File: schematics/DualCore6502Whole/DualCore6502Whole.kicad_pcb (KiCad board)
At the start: 2 copper layers, 72 parts, among them J1 VIN, J2 PWR, J3 PORTA/PORTB, J4 RS232, J5 Bus 1, SW1 Power, SW2 RESET, U1 LM7805, U10 62256, U11 28C256, U12 74HC00, U13 74HC138, U14 74HC374, U15 W65C22N, U16 W65C51N, U17 MAX232, U18 74HC00, U2 W65C02S, U3 74HC157, U4 W65C02S, U5 74HC08, U6 74HC02, U7 74HC32, U8 74HC4017, U9 74HC86, Y1 12MHz, Y2 1.8432MHz

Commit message: Remove the need to multiplex the control lines
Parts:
- removed the C5 at (284.8, 117.5)
- removed the U3 at (149.9, 121.9)
- renumbered C11 to C10, C12 to C11, C13 to C12, C14 to C13, C15 to C14, C16 to C15, C17 to C16, C18 to C17, C19 to C18, C20 to C19, C21 to C20, C22 to C21, C23 to C22, C24 to C23, C6 to C5, C7 to C6, C8 to C7, C9 to C8, C10 to C9, U11 to U10, U12 to U11, U13 to U12, U14 to U13, U15 to U14, U16 to U15, U17 to U16, U18 to U17, U4 to U3, U5 to U4, U6 to U5, U7 to U6, U8 to U7, U9 to U8, U10 to U9
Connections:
- J5 pad 47: SYNC -> unconnected-(J5-Pin_47-Pad47)
- J5 pad 48: ~{VP} -> unconnected-(J5-Pin_48-Pad48)
- U10 pad 1: CPU_ID -> CPU2_BUSEN
- U2 pad 34: CPU1_R/~{W} -> R/~{W}
- U3 pad 34: CPU2_R/~{W} -> R/~{W}
- U6 pad 12: CPU1_CLK -> CPU2_CLK
- U6 pad 13: CPU2_CLK -> CPU1_CLK
- U8 pad 13: CPU_ID -> CPU2_BUSEN

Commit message: Update the schematic
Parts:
- removed the C8 at (277.3, 165.3)
- removed the U4 at (101.6, 45.7)
- added C16: 100nF, Capacitor_THT:C_Disc_D5.0mm_W2.5mm_P5.00mm, F.Cu at (369.1, 177.9)
- added C17: 100nF, Capacitor_THT:C_Disc_D5.0mm_W2.5mm_P5.00mm, F.Cu at (369.1, 181.9)
- added C18: 100nF, Capacitor_THT:C_Disc_D5.0mm_W2.5mm_P5.00mm, F.Cu at (369.1, 186.0)
- added C19: 100nF, Capacitor_THT:C_Disc_D5.0mm_W2.5mm_P5.00mm, F.Cu at (369.1, 190.1)
- added C20: 100nF, Capacitor_THT:C_Disc_D5.0mm_W2.5mm_P5.00mm, F.Cu at (369.1, 194.1)
- added C9: 100nF, Capacitor_THT:C_Disc_D5.0mm_W2.5mm_P5.00mm, F.Cu at (363.2, 203.2)
- added D3: IND4, LED_THT:LED_D3.0mm, F.Cu at (352.4, 174.6)
- added D4: IND3, LED_THT:LED_D3.0mm, F.Cu at (352.4, 180.0)
- added D5: IND2, LED_THT:LED_D3.0mm, F.Cu at (352.4, 185.5)
- added D6: IND1, LED_THT:LED_D3.0mm, F.Cu at (352.4, 191.0)
- added D7: IND0, LED_THT:LED_D3.0mm, F.Cu at (352.4, 196.4)
- added J3: Aux Inputs, Connector_PinHeader_2.54mm:PinHeader_2x05_P2.54mm_Vertical, F.Cu at (396.5, 154.8)
- added JP1: VIA IRQ, Connector_PinHeader_2.54mm:PinHeader_1x03_P2.54mm_Vertical, F.Cu at (374.1, 209.6)
- added JP2: ACIA IRQ, Connector_PinHeader_2.54mm:PinHeader_1x03_P2.54mm_Vertical, F.Cu at (380.7, 209.6)
- added R10: 470R, Resistor_THT:R_Axial_DIN0207_L6.3mm_D2.5mm_P10.16mm_Horizontal, F.Cu at (388.1, 177.9)
- added R11: 470R, Resistor_THT:R_Axial_DIN0207_L6.3mm_D2.5mm_P10.16mm_Horizontal, F.Cu at (388.1, 181.9)
- added R12: 470R, Resistor_THT:R_Axial_DIN0207_L6.3mm_D2.5mm_P10.16mm_Horizontal, F.Cu at (388.1, 186.0)
- added R13: 470R, Resistor_THT:R_Axial_DIN0207_L6.3mm_D2.5mm_P10.16mm_Horizontal, F.Cu at (388.1, 190.1)
- added R5: 1K, Resistor_THT:R_Axial_DIN0207_L6.3mm_D2.5mm_P10.16mm_Horizontal, F.Cu at (373.3, 203.2)
- added R8: 1K, Resistor_THT:R_Axial_DIN0207_L6.3mm_D2.5mm_P10.16mm_Horizontal, F.Cu at (388.6, 203.2)
- added R9: 470R, Resistor_THT:R_Axial_DIN0207_L6.3mm_D2.5mm_P10.16mm_Horizontal, F.Cu at (388.1, 173.8)
- added U14: 74HC259, Package_DIP:DIP-16_W7.62mm, F.Cu at (377.2, 173.9)
- added U15: 74HC245, Package_DIP:DIP-20_W7.62mm, F.Cu at (358.2, 173.9)
- added U16: 74HC00, Package_DIP:DIP-14_W7.62mm, F.Cu at (363.2, 154.5)
- added U17: 74HC08, Package_DIP:DIP-14_W7.62mm, F.Cu at (374.1, 154.5)
- added U18: 74HC74, Package_DIP:DIP-14_W7.62mm, F.Cu at (384.9, 154.5)
- added U7: 74HC138, Package_DIP:DIP-16_W7.62mm, F.Cu at (352.4, 203.2)
- U13: value 74HC374 -> 74HC10; footprint Package_DIP:DIP-20_W7.62mm -> Package_DIP:DIP-14_W7.62mm
- moved U13 315.9 mm to (352.4, 154.5), turned to 0 degrees
- moved J6 287.7 mm to (190.5, 43.2)
- moved C15 152.9 mm to (369.1, 173.8)
- moved U9 86.5 mm to (132.1, 96.5)
- moved U2 61.2 mm to (58.4, 71.1)
- moved SW2 54.1 mm to (57.4, 46.2)
- moved C3 54.1 mm to (53.3, 38.0)
- moved R2 54.1 mm to (53.3, 51.3)
- moved J4 45.0 mm to (45.7, 208.3)
- moved U19 45.0 mm to (53.3, 198.1)
- moved U20 45.0 mm to (119.4, 198.1)
- moved U21 45.0 mm to (162.6, 193.0)
- moved U10 30.6 mm to (68.6, 96.5)
- moved U3 30.6 mm to (116.8, 71.1)
- moved Y1 27.9 mm to (76.2, 45.7)
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- renumbered C16 to C21, C17 to C22, C18 to C23, C19 to C24, C20 to C25, C21 to C26, C22 to C27, C23 to C28, C9 to C8, D3 to D8, D4 to D9, J3 to J4, J4 to J5, J5 to J6, R9 to R14, R10 to R15, R11 to R16, R12 to R17, R13 to R18, R14 to R19, U14 to U19, U15 to U20, U16 to U21, U17 to U22, U5 to U4, U6 to U5, U7 to U6
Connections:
- net Net-(U7-CLK) renamed MAIN_CLK
- D8 pad 2: ~{CPU1_IRQ} -> Net-(D8-A)
- D9 pad 2: ~{CPU2_IRQ} -> Net-(D9-A)
- J5 pad 7: unconnected-(J4-Pad7) -> Net-(U21-R2IN)
- U11 pad 4: A14 -> A15
- U11 pad 5: +5V -> Net-(U11-Pad5)
- U13 pad 1: Net-(U13-OE) -> COMMON_CLK
- U13 pad 10: GND -> Net-(U13-Pad10)
- U13 pad 11: Net-(U13-Cp) -> A8
- U13 pad 12: D4 -> Net-(U15-CE)
- U13 pad 13: D4 -> A7
- U13 pad 14: D5 -> +5V
- U13 pad 2: D0 -> Net-(U13-Pad10)
- U13 pad 3: D0 -> ~{MUTEX_CS}
- U13 pad 4: D1 -> +5V
- U13 pad 5: D1 -> +5V
- U13 pad 6: D2 -> Net-(U13-Pad10)
- U13 pad 7: D2 -> GND
- U13 pad 8: D3 -> Net-(U14-E)
- U13 pad 9: D3 -> COMMON_CLK
- U19 pad 25: CPU1_CLK -> COMMON_CLK
- U20 pad 27: CPU2_CLK -> COMMON_CLK
- U20 pad 8: Net-(U15-~{RTS}) -> unconnected-(U20-~{RTS}-Pad8)
- U21 pad 10: Net-(U15-~{RTS}) -> ~{RTS}
- U21 pad 8: unconnected-(U16-R2IN-Pad8) -> Net-(U21-R2IN)
- U21 pad 9: unconnected-(U16-R2OUT-Pad9) -> ~{CTS}
- U22 pad 13: R/~{W} -> +5V
- U4 pad 10: Net-(U13-Cp) -> unconnected-(U4-Pad10)
- U4 pad 11: R/~{W} -> +5V
- U4 pad 12: GND -> +5V
- U4 pad 13: Net-(U5-Pad13) -> unconnected-(U4-Pad13)
- U4 pad 2: Net-(U4-Pad11) -> BUSEN_RESET
- U4 pad 6: Net-(U4-Pad8) -> BUSEN_SET
- U4 pad 8: ~{MUTEX_CS} -> +5V
- U4 pad 9: R/~{W} -> +5V
- U5 pad 1: ~{CPU1_ML} -> CPU1_CLK_RAW
- U5 pad 10: Net-(U5-Pad13) -> CPU2_CLK_RAW
- U5 pad 12: CPU2_CLK -> CPU2_CLK_RAW
- U5 pad 13: CPU1_CLK -> CPU1_CLK_RAW
- U5 pad 2: ~{MUTEX_CS} -> GND
- U5 pad 3: CPU2_RDY -> CPU1_CLK
- U5 pad 4: ~{CPU2_ML} -> GND
- U5 pad 5: ~{MUTEX_CS} -> GND
- U5 pad 6: CPU1_RDY -> unconnected-(U5-Pad6)
- U5 pad 8: Net-(U13-OE) -> CPU2_CLK
- U5 pad 9: ~{MUTEX_CS} -> GND
- U6 pad 10: CPU2_CLK -> CPU2_CLK_RAW
- U6 pad 2: CPU1_CLK -> CPU1_CLK_RAW
- U8 pad 1: GND -> A14
- U8 pad 10: GND -> +5V
- U8 pad 11: Net-(U9-A14) -> Net-(U9-A9)
- U8 pad 12: A14 -> A9
- U8 pad 13: CPU2_BUSEN -> Net-(U8-Pad13)
- U8 pad 2: GND -> +5V
- U8 pad 3: unconnected-(U8-Pad3) -> Net-(U11-Pad5)
- U8 pad 4: GND -> +5V
- U8 pad 5: GND -> Net-(U11-Pad6)
- U8 pad 6: unconnected-(U8-Pad6) -> IO_CS
- U8 pad 8: unconnected-(U8-Pad8) -> Net-(U8-Pad13)
- U8 pad 9: GND -> Net-(U7-O0)
- U9 pad 1: Net-(U9-A14) -> A14
- U9 pad 24: A9 -> Net-(U9-A9)
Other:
- board outline added: 160 x 121.9 mm

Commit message: Basic PCB layout
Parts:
- removed the C2 at (390.9, 43.1)
- removed the D1 at (377.9, 38.9)
- removed the U1 at (367.7, 44.4)
- added C28: 10nF, Capacitor_THT:C_Disc_D5.0mm_W2.5mm_P5.00mm, F.Cu at (143.5, 39.5)
- added C29: 100nF, Capacitor_THT:C_Disc_D5.0mm_W2.5mm_P5.00mm, F.Cu at (158.8, 38.1)
- added JP3: NMI2, Connector_PinHeader_2.54mm:PinHeader_1x02_P2.54mm_Vertical, F.Cu at (142.2, 73.7)
- added R20: 5K6, Resistor_THT:R_Axial_DIN0207_L6.3mm_D2.5mm_P10.16mm_Horizontal, F.Cu at (171.4, 47.0)
- added R21: 2K2, Resistor_THT:R_Axial_DIN0207_L6.3mm_D2.5mm_P10.16mm_Horizontal, F.Cu at (167.6, 36.8)
- added RV1: 10K, Potentiometer_THT:Potentiometer_Bourns_3266Y_Vertical, F.Cu at (163.8, 44.4)
- added TP1: CPU1 SYNC, TestPoint:TestPoint_Pad_D1.5mm, F.Cu at (57.1, 69.9)
- added TP2: ~{CPU1_VP}, TestPoint:TestPoint_Pad_D1.5mm, F.Cu at (64.8, 69.9)
- added TP3: ~{CPU1_ML}, TestPoint:TestPoint_Pad_D1.5mm, F.Cu at (61.0, 69.9)
- added TP4: CPU2 SYNC, TestPoint:TestPoint_Pad_D1.5mm, F.Cu at (120.7, 69.9)
- added TP5: ~{CPU2_VP}, TestPoint:TestPoint_Pad_D1.5mm, F.Cu at (128.3, 69.9)
- added TP6: ~{CPU2_ML}, TestPoint:TestPoint_Pad_D1.5mm, F.Cu at (124.5, 69.9)
- added TP7: 1KHz, TestPoint:TestPoint_Pad_D1.5mm, F.Cu at (152.4, 49.5)
- added U22: 7555, Package_DIP:DIP-8_W7.62mm_Socket, F.Cu at (147.3, 45.7)
- C1: value 47uF -> 100uF
- D1: renamed from D2; value Power On -> Power
- J1: value VIN -> 5VDC
- J2: footprint Connector_PinHeader_2.54mm:PinHeader_1x04_P2.54mm_Vertical -> Connector_Phoenix_MC_HighVoltage:PhoenixContact_MC_1,5_3-G-5.08_1x03_P5.08mm_Horizontal
- J6: value Bus 1 -> RCBus; footprint RCBus:RCBus_PinSocket_2x40_P2.54mm_Vertical -> RCBus:RCBus_PinSocket_2x40_P2.54mm_Vertical_DC
- JP2: value ACIA IRQ -> NMI1; footprint Connector_PinHeader_2.54mm:PinHeader_1x03_P2.54mm_Vertical -> Connector_PinHeader_2.54mm:PinHeader_1x02_P2.54mm_Vertical
- R1: value 220R -> 470R
- SW1: value Power -> Power On
- U1: renamed from U2; footprint Package_DIP:DIP-40_W15.24mm -> Package_DIP:DIP-40_W15.24mm_Socket
- U10: renamed from U11; footprint Package_DIP:DIP-14_W7.62mm -> Package_DIP:DIP-14_W7.62mm_Socket
- U11: renamed from U12; footprint Package_DIP:DIP-16_W7.62mm -> Package_DIP:DIP-16_W7.62mm_Socket
- U12: renamed from U13; footprint Package_DIP:DIP-14_W7.62mm -> Package_DIP:DIP-14_W7.62mm_Socket
- U13: renamed from U14; footprint Package_DIP:DIP-16_W7.62mm -> Package_DIP:DIP-16_W7.62mm_Socket
- U14: renamed from U15; footprint Package_DIP:DIP-20_W7.62mm -> Package_DIP:DIP-20_W7.62mm_Socket
- U15: renamed from U16; footprint Package_DIP:DIP-14_W7.62mm -> Package_DIP:DIP-14_W7.62mm_Socket
- U16: renamed from U17; footprint Package_DIP:DIP-14_W7.62mm -> Package_DIP:DIP-14_W7.62mm_Socket
- U17: renamed from U18; footprint Package_DIP:DIP-14_W7.62mm -> Package_DIP:DIP-14_W7.62mm_Socket
- U18: renamed from U19; footprint Package_DIP:DIP-40_W15.24mm -> Package_DIP:DIP-40_W15.24mm_Socket
- U19: renamed from U20; footprint Package_DIP:DIP-28_W15.24mm -> Package_DIP:DIP-28_W15.24mm_Socket
- U2: renamed from U3; footprint Package_DIP:DIP-40_W15.24mm -> Package_DIP:DIP-40_W15.24mm_Socket
- U20: renamed from U21; footprint Package_DIP:DIP-16_W7.62mm -> Package_DIP:DIP-16_W7.62mm_Socket
- U21: renamed from U22; footprint Package_DIP:DIP-14_W7.62mm -> Package_DIP:DIP-14_W7.62mm_Socket
- U3: renamed from U5; footprint Package_DIP:DIP-14_W7.62mm -> Package_DIP:DIP-14_W7.62mm_Socket
- U4: footprint Package_DIP:DIP-14_W7.62mm -> Package_DIP:DIP-14_W7.62mm_Socket
- U5: renamed from U6; footprint Package_DIP:DIP-16_W7.62mm -> Package_DIP:DIP-16_W7.62mm_Socket
- U6: renamed from U7; footprint Package_DIP:DIP-16_W7.62mm -> Package_DIP:DIP-16_W7.62mm_Socket
- U7: renamed from U8; footprint Package_DIP:DIP-14_W7.62mm -> Package_DIP:DIP-14_W7.62mm_Socket
- U8: renamed from U9; footprint Package_DIP:DIP-28_W15.24mm -> Package_DIP:DIP-28_W15.24mm_Socket
- Y2: footprint Crystal:Crystal_HC49-U_Horizontal -> Crystal:Crystal_HC49-U_Vertical
- moved Y2 405.1 mm to (67.3, 128.3), turned to 180 degrees
- moved D8 398.9 mm to (53.3, 55.9), turned to -90 degrees
- moved C22 397.2 mm to (52.1, 128.3)
- moved SW1 367.6 mm to (34.3, 129.5)
- moved J1 365.3 mm to (44.5, 146.4)
- moved J5 363.0 mm to (127.7, 152.7)
- moved C21 359.6 mm to (87.6, 111.7), turned to 90 degrees
- moved C23 355.7 mm to (91.5, 119.4)
- moved C26 353.4 mm to (91.5, 123.2)
- moved R5 348.8 mm to (57.1, 55.9), turned to -90 degrees
- moved C24 348.4 mm to (99.1, 123.2)
- moved R14 346.3 mm to (82.5, 128.3), turned to 180 degrees
- moved C25 346.1 mm to (99.1, 119.4)
- moved J2 343.8 mm to (39.4, 109.2), turned to -90 degrees
- moved H4 343.4 mm to (34.3, 157.5)
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- renumbered C11 to C10, C12 to C11, C13 to C12, C14 to C13, C15 to C14, C16 to C15, C17 to C16, C18 to C17, C19 to C18, C20 to C19, C3 to C2, C21 to C20, C22 to C21, C23 to C22, C24 to C23, C25 to C24, C26 to C25, C27 to C26, C28 to C27, C4 to C3, C5 to C4, C6 to C5, C7 to C6, C8 to C7, C9 to C8, C10 to C9, D3 to D2, D4 to D3, D5 to D4, D6 to D5, D7 to D6, D8 to D7, D9 to D8, U10 to U9
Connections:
- C1 pad 1: Net-(D1-K) -> +5V
- D8 pad 2: Net-(D9-A) -> ~{CPU1_IRQ}
- J2 pad 1: VDD -> +5V
- J2 pad 2: +5V -> ~{RESET}
- J2 pad 3: ~{RESET} -> GND
- J6 pad 35: unconnected-(J6-Pin_35-Pad35) -> TX
- J6 pad 36: unconnected-(J6-Pin_36-Pad36) -> RX
- J6 pad 41: ~{VIA_CS} -> MAIN_CLK
- J6 pad 42: ~{ACIA_CS} -> CPU1_CLK
- J6 pad 43: ~{IO_4_CS} -> CPU2_CLK
- J6 pad 44: ~{IO_5_CS} -> unconnected-(J6-Pin_44-Pad44)
- J6 pad 45: ~{IO_6_CS} -> ~{IO_4_CS}
- J6 pad 46: ~{IO_7_CS} -> ~{IO_5_CS}
- J6 pad 47: unconnected-(J6-Pin_47-Pad47) -> ~{IO_6_CS}
- J6 pad 48: unconnected-(J6-Pin_48-Pad48) -> ~{IO_7_CS}
- J6 pad 78: CPU1_CLK -> ~{VIA_CS}
- J6 pad 79: CPU2_CLK -> ~{ACIA_CS}
- JP2 pad 1: ~{CPU1_IRQ} -> Net-(JP2-A)
- JP2 pad 2: Net-(D9-A) -> ~{CPU1_NMI}
- SW1 pad 1: VDD -> +5V
- U1 pad 1: ~{CPU1_VP} -> Net-(U1-~{VP})
- U1 pad 5: ~{CPU1_ML} -> Net-(U1-~{ML})
- U1 pad 7: CPU1_SYNC -> Net-(U1-SYNC)
- U11 pad 4: A13 -> A12
- U11 pad 5: A12 -> A13
- U13 pad 10: Net-(U14-Q5) -> Net-(U13-Q5)
- U15 pad 1: +5V -> MUTEX_WANT1
- U15 pad 10: +5V -> Net-(U13-Q5)
- U15 pad 11: ~{RTS} -> unconnected-(U15-Pad11)
- U15 pad 12: Net-(U14-Q5) -> +5V
- U15 pad 2: +5V -> MUTEX_WANT2
- U15 pad 3: unconnected-(U16-Pad3) -> Net-(U15-Pad3)
- U15 pad 4: MUTEX_WANT1 -> +5V
- U15 pad 5: MUTEX_WANT2 -> +5V
- U15 pad 6: Net-(U16-Pad6) -> unconnected-(U15-Pad6)
- U15 pad 8: unconnected-(U16-Pad8) (its old number) -> ~{RTS}
- U16 pad 2: Net-(U16-Pad6) -> Net-(U15-Pad3)
- U19 pad 10: Net-(U20-TxD) -> TX
- U19 pad 12: Net-(U20-RxD) -> RX
- U2 pad 1: ~{CPU2_VP} -> Net-(U2-~{VP})
- U2 pad 5: ~{CPU2_ML} -> Net-(U2-~{ML})
- U2 pad 7: CPU2_SYNC -> Net-(U2-SYNC)
- U20 pad 11: Net-(U20-TxD) -> TX
- U20 pad 12: Net-(U20-RxD) -> RX
- U4 pad 10: unconnected-(U4-Pad10) -> Net-(JP3-A)
- U4 pad 11: +5V -> Net-(U22-Q)
- U4 pad 12: +5V -> GND
- U4 pad 13: unconnected-(U4-Pad13) -> Net-(JP2-A)
- U4 pad 8: +5V -> GND
- U4 pad 9: +5V -> Net-(U22-Q)
- U6 pad 15: Net-(U7-O0) -> Net-(U6-O0)
- U6 pad 4: A14 -> A13
- U6 pad 5: A13 -> A14
- U7 pad 10: +5V -> Net-(U7-Pad10)
- U7 pad 11: Net-(U9-A9) -> Net-(U7-Pad10)
- U7 pad 12: A9 -> Net-(U6-O0)
- U7 pad 13: Net-(U8-Pad13) -> +5V
- U7 pad 8: Net-(U8-Pad13) -> Net-(U8-A9)
- U7 pad 9: Net-(U7-O0) -> A9
- U8 pad 24: Net-(U9-A9) -> Net-(U8-A9)
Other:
- board size 160 x 121.9 mm -> 170.2 x 127 mm
- copper layers 2 -> 4
- board text added: "1"
- board text added: "2"
- board text added: "5V"
- board text added: "CA1"
- board text added: "CA2"
- board text added: "CB1"
- board text added: "CB2"
- board text added: "Dual Core 65C02 Computer by Rhys Weatherley, 2026"
- board text added: "GND"
- board text added: "INP"
- board text added: "PA0"
- board text added: "PA1"
- board text added: "PA2"
- board text added: "PA3"
- board text added: "PA4"
- board text added: "PA5"
- board text added: "PA6"
- board text added: "PA7"
- board text added: "PB0"
- board text added: "PB1"
- board text added: "PB2"
- board text added: "PB3"
- board text added: "PB4"
- board text added: "PB5"
- board text added: "PB6"
- board text added: "PB7"
- board text added: "~{RESET}"

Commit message: Power planes
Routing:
- net Net-(SW1-B): track 0.00 -> 20.0 mm
- added copper zone on In2.Cu, net +5V
- added copper zone on In1.Cu, net GND
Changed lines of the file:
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@@
+		)
+	)
+	(segment
+		(start 44.45 146.3625)
+		(end 43.133362 146.3625)
+		(width 2)
+		(layer "B.Cu")
+		(net 18)
+	)
+	(segment
+		(start 38.1 134.687919)
+		(end 35.492081 132.08)
+		(width 2)
+		(layer "B.Cu")
+		(net 18)
+	)
+	(segment
+		(start 38.1 141.329138)
+		(end 38.1 134.687919)
+		(width 2)
+		(layer "B.Cu")
+		(net 18)
+	)
+	(segment
+		(start 43.133362 146.3625)
+		(end 38.1 141.329138)
+		(width 2)
+		(layer "B.Cu")
+		(net 18)
+	)
+	(segment
+		(start 35.492081 132.08)
+		(end 34.29 132.08)
+		(width 2)
+		(layer "B.Cu")
+		(net 18)
+	)
+	(zone
+		(net 1)
+		(net_name "GND")
+		(layer "In1.Cu")
+		(hatch edge 0.5)
+		(connect_pads
+			(clearance 0.5)
+		)
+		(min_thickness 0.25)
+		(filled_areas_thickness no)
+		(fill yes
+			(thermal_gap 0.5)
+			(thermal_bridge_width 0.5)
+		)
+		(polygon
+			(pts
+				(xy 30.48 34.29) (xy 200.66 34.29) (xy 200.66 161.29) (xy 30.48 161.29)
+			)
+		)
+	)
+	(zone
+		(net 3)
+		(net_name "+5V")
+		(layer "In2.Cu")
+		(hatch edge 0.5)
+		(priority 1)
+		(connect_pads
+			(clearance 0.5)
+		)
+		(min_thickness 0.25)
+		(filled_areas_thickness no)
+		(fill yes
+			(thermal_gap 0.5)
+			(thermal_bridge_width 0.5)
+		)
+		(polygon
+			(pts
+				(xy 30.48 34.29) (xy 200.66 34.29) (xy 200.66 161.29) (xy 30.48 161.29)
+			)
 		)
 	)

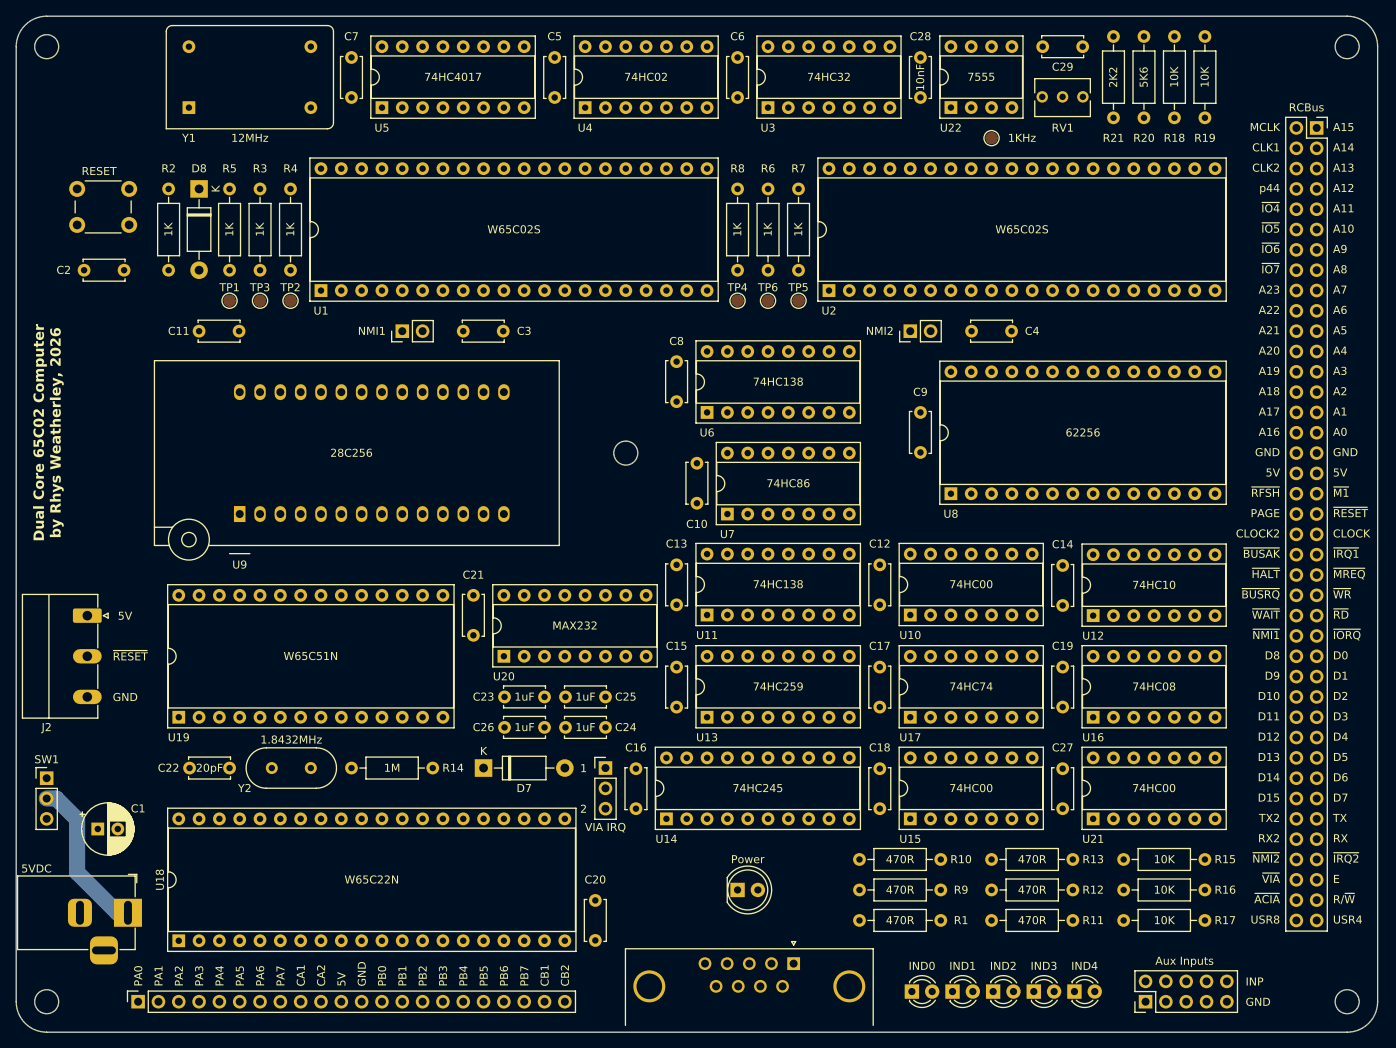
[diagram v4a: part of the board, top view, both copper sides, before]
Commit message: Route the PCB
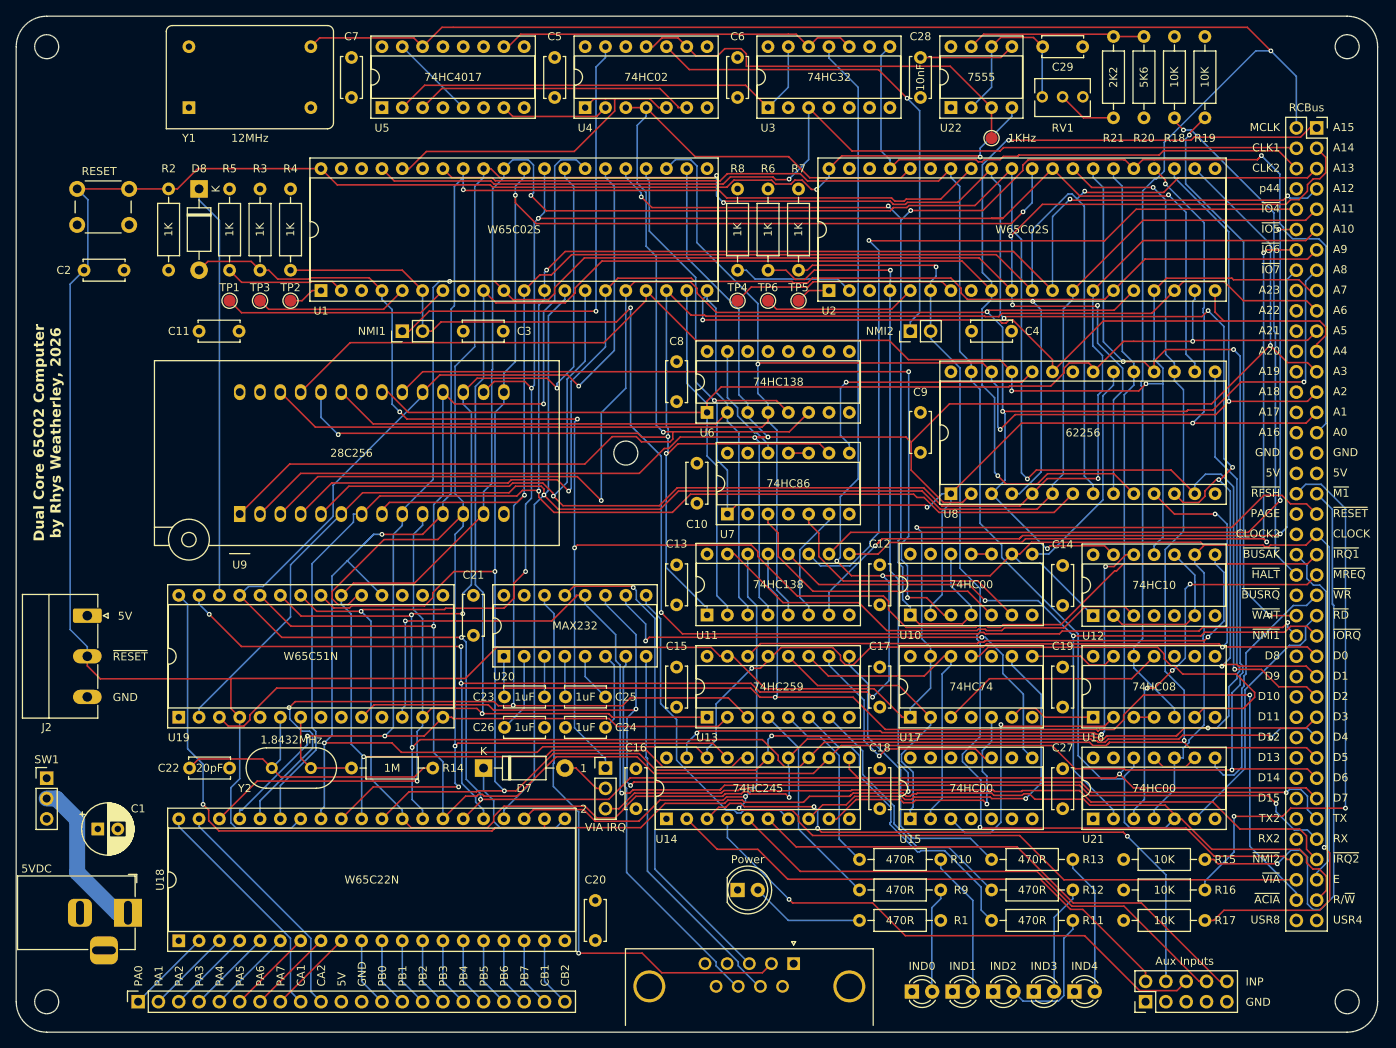
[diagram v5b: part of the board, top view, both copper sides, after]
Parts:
- moved C24 5.00 mm to (104.1, 123.2), turned to 180 degrees
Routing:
- net ~{RESET}: track 0.00 -> 403.7 mm, vias 0 -> 3
- net COMMON_CLK: track 0.00 -> 353.8 mm, vias 0 -> 6
- net D4: track 0.00 -> 352.5 mm, vias 0 -> 7
- net R/~{W}: track 0.00 -> 351.6 mm, vias 0 -> 1
- net D3: track 0.00 -> 350.2 mm, vias 0 -> 6
- net D1: track 0.00 -> 338.9 mm, vias 0 -> 9
- net D6: track 0.00 -> 338.0 mm, vias 0 -> 5
- net D0: track 0.00 -> 331.9 mm, vias 0 -> 6
- net D7: track 0.00 -> 328.4 mm, vias 0 -> 4
- net A0: track 0.00 -> 323.0 mm, vias 0 -> 4
- net D5: track 0.00 -> 322.1 mm, vias 0 -> 6
- net D2: track 0.00 -> 320.4 mm, vias 0 -> 4
- net A2: track 0.00 -> 301.1 mm, vias 0 -> 4
- net A1: track 0.00 -> 297.0 mm, vias 0 -> 6
- net A3: track 0.00 -> 276.2 mm, vias 0 -> 4
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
